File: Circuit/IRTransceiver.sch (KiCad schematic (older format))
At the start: 0 parts

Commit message: IR receiver schematic & footprint.
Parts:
- added P?: IRReceiver, symbol CONN_01X03
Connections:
- new net +3V3: P?.3 (P3)
- new net GND: P?.2 (P2)
- new net IRRx: P?.1 (P1)
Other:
- note added: "Out"
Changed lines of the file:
@@
 $Descr A4 11693 8268
 encoding utf-8
-Sheet 1 7
+Sheet 7 7
 Title ""
 Date ""
@@
 Comment4 ""
 $EndDescr
+$Comp
+L CONN_01X03 P?
+U 1 1 581D5ECE
+P 4600 2700
+F 0 "P?" H 4600 2900 50  0000 C CNN
+F 1 "IRReceiver" V 4700 2700 50  0000 C CNN
+F 2 "" H 4600 2700 50  0000 C CNN
+F 3 "" H 4600 2700 50  0000 C CNN
+F 4 "TSOP38238" H 4600 2700 60  0001 C CNN "Manufacturer PN"
+F 5 "751-1227-ND" H 4600 2700 60  0001 C CNN "Digikey PN"
+F 6 "http://www.digikey.com.au/product-detail/en/vishay-semiconductor-opto-division/TSOP38238/751-1227-ND/1681362" H 4600 2700 60  0001 C CNN "Link"
+F 7 "1.12" H 4600 2700 60  0001 C CNN "Unit Cost"
+	1    4600 2700
+	1    0    0    -1
+$EndComp
+$Comp
+L +3.3V #PWR?
+U 1 1 581D5F60
+P 4050 2750
+F 0 "#PWR?" H 4050 2600 50  0001 C CNN
+F 1 "+3.3V" H 4050 2890 50  0000 C CNN
+F 2 "" H 4050 2750 50  0000 C CNN
+F 3 "" H 4050 2750 50  0000 C CNN
+	1    4050 2750
+	1    0    0    -1
+$EndComp
+$Comp
+L GND #PWR?
+U 1 1 581D5F76
+P 4250 2750
+F 0 "#PWR?" H 4250 2500 50  0001 C CNN
+F 1 "GND" H 4250 2600 50  0000 C CNN
+F 2 "" H 4250 2750 50  0000 C CNN
+F 3 "" H 4250 2750 50  0000 C CNN
+	1    4250 2750
+	1    0    0    -1
+$EndComp
+Text Notes 4400 2450 0    60   ~ 0
+Out
+Text HLabel 4050 2500 0    60   Input ~ 0
+IRRx
+Wire Wire Line
+	4400 2700 4250 2700
+Wire Wire Line
+	4250 2700 4250 2750
+Wire Wire Line
+	4400 2800 4400 2950
+Wire Wire Line
+	4400 2950 4050 2950
+Wire Wire Line
+	4050 2950 4050 2750
+Wire Wire Line
+	4400 2600 4400 2500
+Wire Wire Line
+	4400 2500 4050 2500
 $EndSCHEMATC

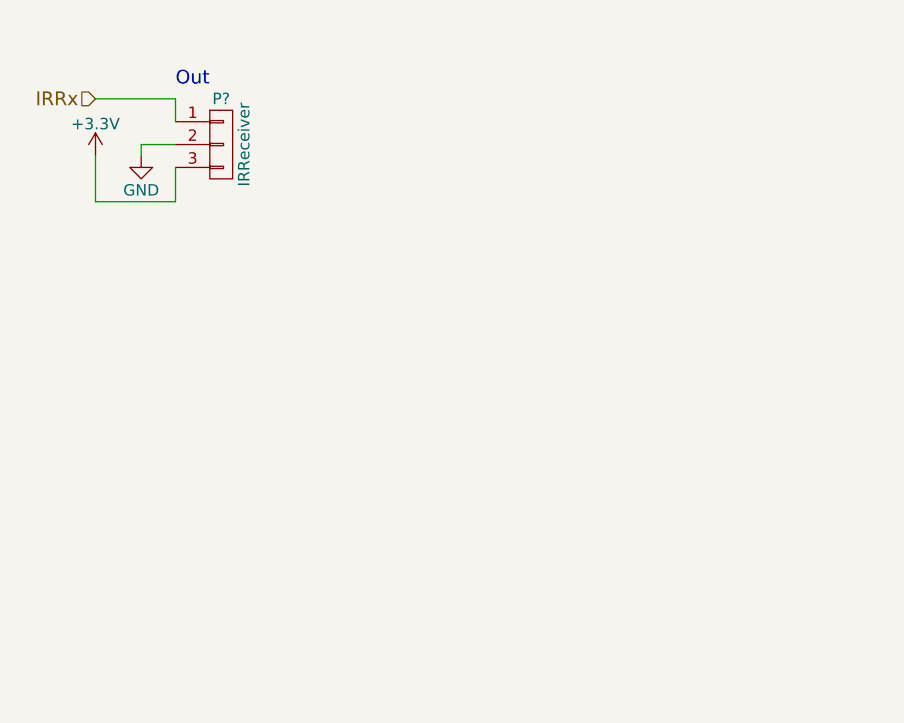
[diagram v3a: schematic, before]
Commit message: IRTx & forward slashing the fp-lib-table.
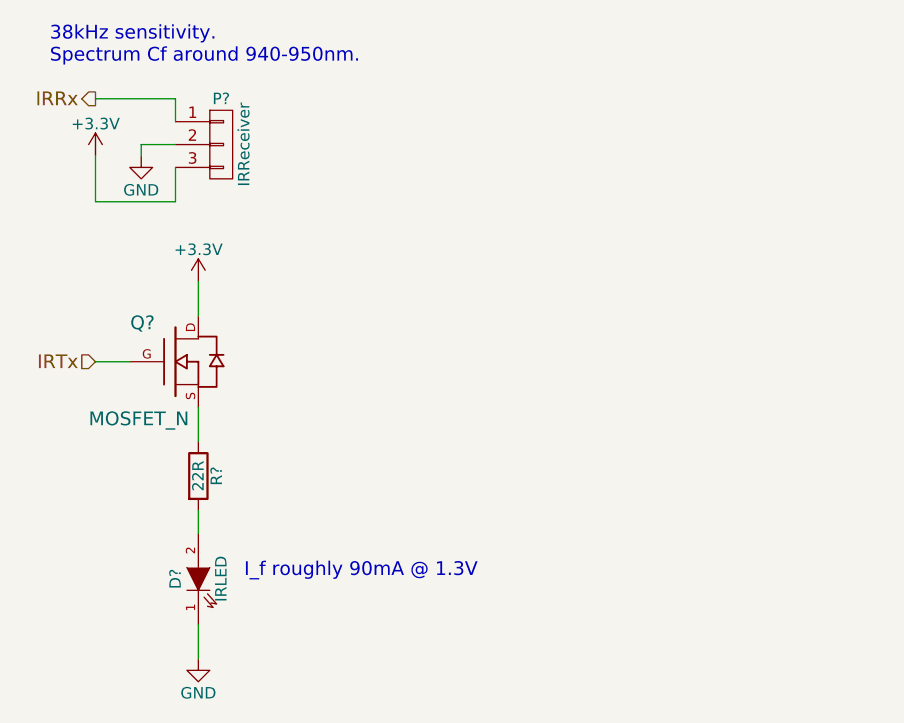
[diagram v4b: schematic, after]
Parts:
- added D?: IRLED, LEDs:LED-5MM, symbol LED
- added Q?: MOSFET_N, symbol MOSFET_N
- added R?: 22R, Resistors_SMD:R_0603_HandSoldering, symbol R
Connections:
- net +3V3: now also Q?.D
- net GND: now also D?.1 (K)
- new net: D?.2 (A), R?.2
- new net: Q?.S, R?.1
- new net IRTx: Q?.G
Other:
- note added: "38kHz sensitivity. \nSpectrum Cf around 940-950nm."
- note added: "I_f roughly 90mA @ 1.3V"
- note removed: "Out"
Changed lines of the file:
@@
 	1    0    0    -1
 $EndComp
-Text Notes 4400 2450 0    60   ~ 0
-Out
-Text HLabel 4050 2500 0    60   Input ~ 0
+Text Notes 3850 2350 0    60   ~ 0
+38kHz sensitivity. \nSpectrum Cf around 940-950nm.
+Text HLabel 4050 2500 0    60   Output ~ 0
 IRRx
 Wire Wire Line
@@
 	4400 2950 4050 2950
 Wire Wire Line
-	4050 2950 4050 2750
-Wire Wire Line
 	4400 2600 4400 2500
 Wire Wire Line
 	4400 2500 4050 2500
+$Comp
+L LED D?
+U 1 1 581D68B3
+P 4500 4600
+F 0 "D?" H 4500 4700 50  0000 C CNN
+F 1 "IRLED" H 4500 4500 50  0000 C CNN
+F 2 "LEDs:LED-5MM" H 4500 4600 50  0001 C CNN
+F 3 "" H 4500 4600 50  0000 C CNN
+F 4 "TSAL6200" H 4500 4600 60  0001 C CNN "Manufacturer PN"
+F 5 "751-1204-ND" H 4500 4600 60  0001 C CNN "Digikey PN"
+F 6 "http://www.digikey.com.au/product-detail/en/vishay-semiconductor-opto-division/TSAL6200/751-1204-ND/1681339" H 4500 4600 60  0001 C CNN "Link"
+F 7 "0.57" H 4500 4600 60  0001 C CNN "Unit Cost"
+	1    4500 4600
+	0    -1   -1   0
+$EndComp
+$Comp
+L R R?
+U 1 1 581D690A
+P 4500 4150
+F 0 "R?" V 4580 4150 50  0000 C CNN
+F 1 "22R" V 4500 4150 50  0000 C CNN
+F 2 "Resistors_SMD:R_0603_HandSoldering" V 4430 4150 50  0001 C CNN
+F 3 "" H 4500 4150 50  0000 C CNN
+	1    4500 4150
+	1    0    0    -1
+$EndComp
+Wire Wire Line
+	4500 4300 4500 4400
+$Comp
+L MOSFET_N Q?
+U 1 1 581D6A1D
+P 4400 3650
+F 0 "Q?" H 4310 3820 60  0000 R CNN
+F 1 "MOSFET_N" H 4460 3400 60  0000 R CNN
+F 2 "" H 4400 3650 60  0000 C CNN
+F 3 "" H 4400 3650 60  0000 C CNN
+	1    4400 3650
+	1    0    0    -1
+$EndComp
+Wire Wire Line
+	4500 3850 4500 4000
+$Comp
+L GND #PWR?
+U 1 1 581D6BBC
+P 4500 4950
+F 0 "#PWR?" H 4500 4700 50  0001 C CNN
+F 1 "GND" H 4500 4800 50  0000 C CNN
+F 2 "" H 4500 4950 50  0000 C CNN
+F 3 "" H 4500 4950 50  0000 C CNN
+	1    4500 4950
+	1    0    0    -1
+$EndComp
+Wire Wire Line
+	4500 4800 4500 4950
+Wire Wire Line
+	4050 2950 4050 2750
+$Comp
+L +3.3V #PWR?
+U 1 1 581D6BFC
+P 4500 3300
+F 0 "#PWR?" H 4500 3150 50  0001 C CNN
+F 1 "+3.3V" H 4500 3440 50  0000 C CNN
+F 2 "" H 4500 3300 50  0000 C CNN
+F 3 "" H 4500 3300 50  0000 C CNN
+	1    4500 3300
+	1    0    0    -1
+$EndComp
+Wire Wire Line
+	4500 3300 4500 3450
+Text HLabel 4050 3650 0    60   Input ~ 0
+IRTx
+Wire Wire Line
+	4050 3650 4200 3650
+Text Notes 4700 4600 0    60   ~ 0
+I_f roughly 90mA @ 1.3V
 $EndSCHEMATC

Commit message: Reference documents added & renamed to be more descriptive.
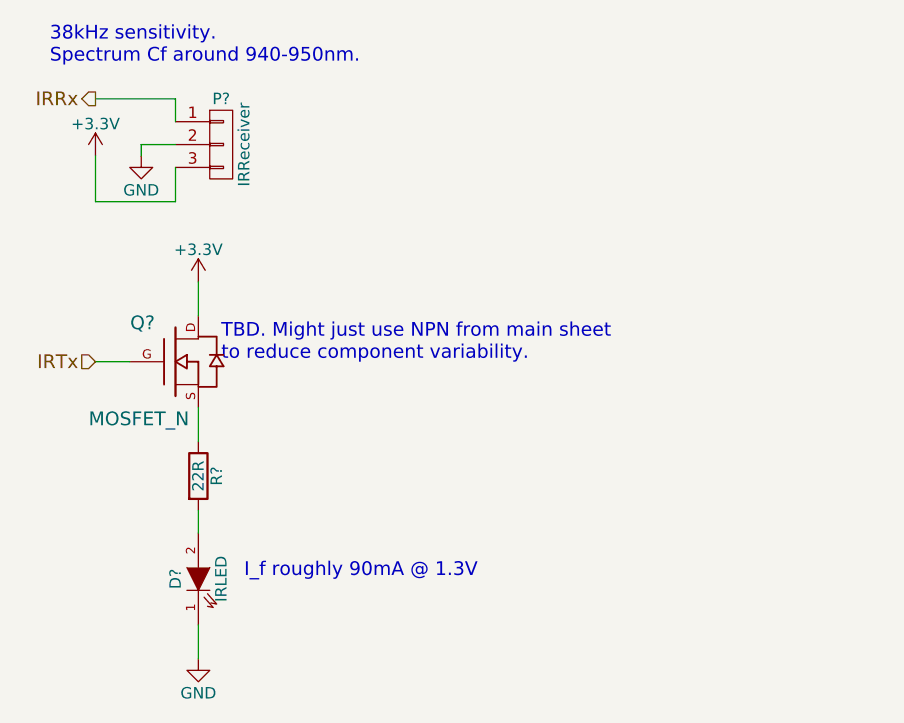
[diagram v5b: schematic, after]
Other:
- note added: "TBD. Might just use NPN from main sheet\nto reduce component variability."
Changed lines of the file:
@@
 Text Notes 4700 4600 0    60   ~ 0
 I_f roughly 90mA @ 1.3V
+Text Notes 4600 3650 0    60   ~ 0
+TBD. Might just use NPN from main sheet\nto reduce component variability.
 $EndSCHEMATC

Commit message: Messing with John's layout. You're welcome.
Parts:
- removed Q?: MOSFET_N, symbol MOSFET_N
- added Q?: S8050, TO_SOT_Packages_SMD:SOT-23_Handsoldering, symbol S8050
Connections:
- net +3V3: now also Q?.3 (C)
- net IRTx: now also Q?.2 (B)
- net at R?.1: now also Q?.1 (E)
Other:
- note added: "Lazy, but we don't have any N-MOS on the design\nand will work just fine."
- note removed: "TBD. Might just use NPN from main sheet\nto reduce component variability."
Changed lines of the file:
@@
 Wire Wire Line
 	4500 4300 4500 4400
-$Comp
-L MOSFET_N Q?
-U 1 1 581D6A1D
-P 4400 3650
-F 0 "Q?" H 4310 3820 60  0000 R CNN
-F 1 "MOSFET_N" H 4460 3400 60  0000 R CNN
-F 2 "" H 4400 3650 60  0000 C CNN
-F 3 "" H 4400 3650 60  0000 C CNN
-	1    4400 3650
-	1    0    0    -1
-$EndComp
 Wire Wire Line
 	4500 3850 4500 4000
@@
 Text Notes 4700 4600 0    60   ~ 0
 I_f roughly 90mA @ 1.3V
-Text Notes 4600 3650 0    60   ~ 0
-TBD. Might just use NPN from main sheet\nto reduce component variability.
+Text Notes 4750 3600 0    60   ~ 0
+Lazy, but we don't have any N-MOS on the design\nand will work just fine.
+$Comp
+L S8050 Q?
+U 1 1 581E1075
+P 4400 3650
+F 0 "Q?" H 4600 3725 50  0000 L CNN
+F 1 "S8050" H 4600 3650 50  0000 L CNN
+F 2 "TO_SOT_Packages_SMD:SOT-23_Handsoldering" H 4600 3575 50  0000 L CIN
+F 3 "" H 4400 3650 50  0000 L CNN
+	1    4400 3650
+	1    0    0    -1
+$EndComp
 $EndSCHEMATC

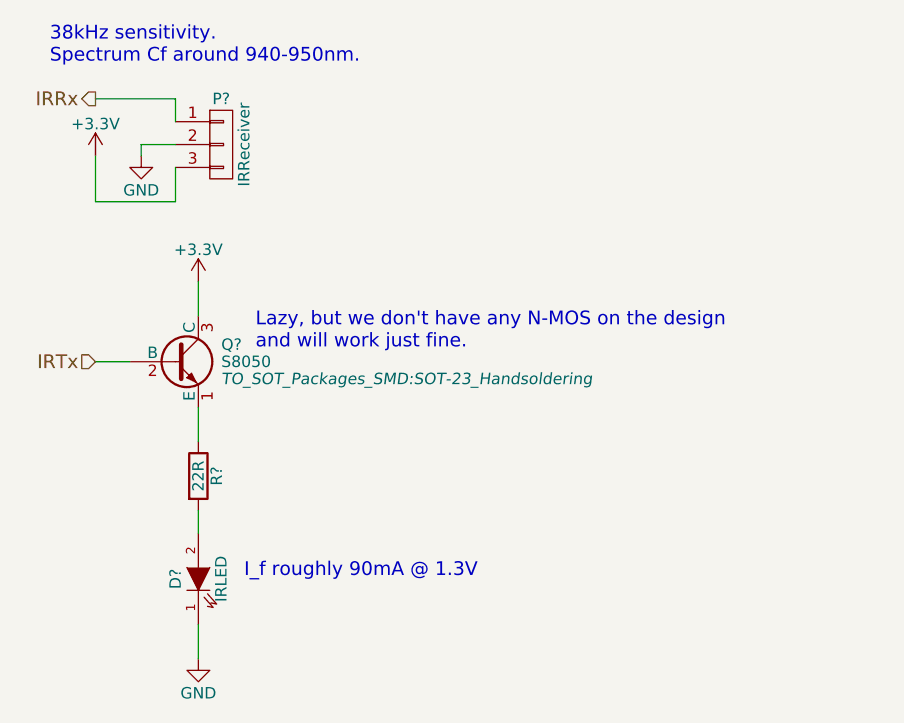
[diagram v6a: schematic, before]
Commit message: Removed PRGM button. placed some components.
PGRM button can be performed by joystick.
CHRG led removed.
placed some components.
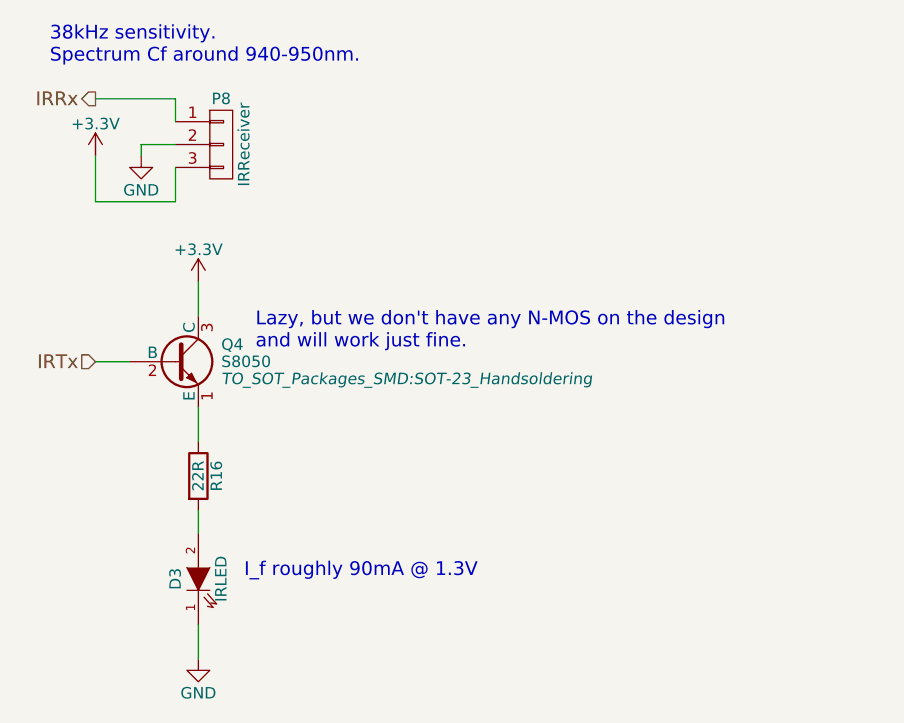
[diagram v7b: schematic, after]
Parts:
- gave numbers to parts that had none: 4
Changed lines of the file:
@@
 $EndDescr
 $Comp
-L CONN_01X03 P?
+L CONN_01X03 P8
 U 1 1 581D5ECE
 P 4600 2700
-F 0 "P?" H 4600 2900 50  0000 C CNN
+F 0 "P8" H 4600 2900 50  0000 C CNN
 F 1 "IRReceiver" V 4700 2700 50  0000 C CNN
 F 2 "" H 4600 2700 50  0000 C CNN
@@
 $EndComp
 $Comp
-L +3.3V #PWR?
+L +3.3V #PWR066
 U 1 1 581D5F60
 P 4050 2750
-F 0 "#PWR?" H 4050 2600 50  0001 C CNN
+F 0 "#PWR066" H 4050 2600 50  0001 C CNN
 F 1 "+3.3V" H 4050 2890 50  0000 C CNN
 F 2 "" H 4050 2750 50  0000 C CNN
@@
 $EndComp
 $Comp
-L GND #PWR?
+L GND #PWR067
 U 1 1 581D5F76
 P 4250 2750
-F 0 "#PWR?" H 4250 2500 50  0001 C CNN
+F 0 "#PWR067" H 4250 2500 50  0001 C CNN
 F 1 "GND" H 4250 2600 50  0000 C CNN
 F 2 "" H 4250 2750 50  0000 C CNN
@@
 	4400 2500 4050 2500
 $Comp
-L LED D?
+L LED D3
 U 1 1 581D68B3
 P 4500 4600
-F 0 "D?" H 4500 4700 50  0000 C CNN
+F 0 "D3" H 4500 4700 50  0000 C CNN
 F 1 "IRLED" H 4500 4500 50  0000 C CNN
 F 2 "LEDs:LED-5MM" H 4500 4600 50  0001 C CNN
@@
 $EndComp
 $Comp
-L R R?
+L R R16
 U 1 1 581D690A
 P 4500 4150
-F 0 "R?" V 4580 4150 50  0000 C CNN
+F 0 "R16" V 4580 4150 50  0000 C CNN
 F 1 "22R" V 4500 4150 50  0000 C CNN
 F 2 "Resistors_SMD:R_0603_HandSoldering" V 4430 4150 50  0001 C CNN
@@
 	4500 3850 4500 4000
 $Comp
-L GND #PWR?
+L GND #PWR068
 U 1 1 581D6BBC
 P 4500 4950
-F 0 "#PWR?" H 4500 4700 50  0001 C CNN
+F 0 "#PWR068" H 4500 4700 50  0001 C CNN
 F 1 "GND" H 4500 4800 50  0000 C CNN
 F 2 "" H 4500 4950 50  0000 C CNN
@@
 	4050 2950 4050 2750
 $Comp
-L +3.3V #PWR?
+L +3.3V #PWR069
 U 1 1 581D6BFC
 P 4500 3300
-F 0 "#PWR?" H 4500 3150 50  0001 C CNN
+F 0 "#PWR069" H 4500 3150 50  0001 C CNN
 F 1 "+3.3V" H 4500 3440 50  0000 C CNN
 F 2 "" H 4500 3300 50  0000 C CNN
@@
 Lazy, but we don't have any N-MOS on the design\nand will work just fine.
 $Comp
-L S8050 Q?
+L S8050 Q4
 U 1 1 581E1075
 P 4400 3650
-F 0 "Q?" H 4600 3725 50  0000 L CNN
+F 0 "Q4" H 4600 3725 50  0000 L CNN
 F 1 "S8050" H 4600 3650 50  0000 L CNN
 F 2 "TO_SOT_Packages_SMD:SOT-23_Handsoldering" H 4600 3575 50  0000 L CIN

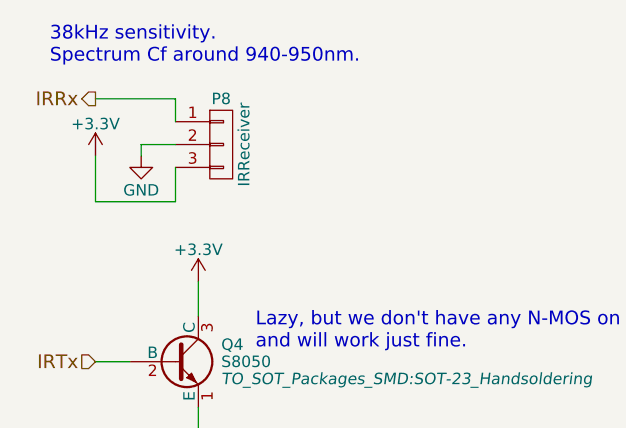
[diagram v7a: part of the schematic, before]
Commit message: Footprint assigned for IR receiver.
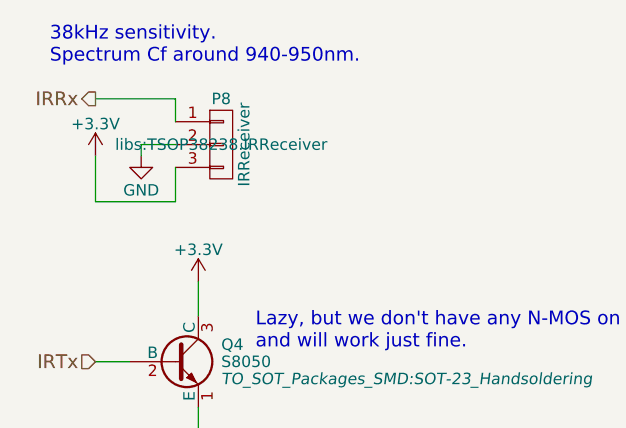
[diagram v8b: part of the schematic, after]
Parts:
- P8: footprint (none) -> libs:TSOP38238.IRReceiver
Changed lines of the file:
@@
 F 0 "P8" H 4600 2900 50  0000 C CNN
 F 1 "IRReceiver" V 4700 2700 50  0000 C CNN
-F 2 "" H 4600 2700 50  0000 C CNN
+F 2 "libs:TSOP38238.IRReceiver" H 4600 2700 50  0000 C CNN
 F 3 "" H 4600 2700 50  0000 C CNN
 F 4 "TSOP38238" H 4600 2700 60  0001 C CNN "Manufacturer PN"
